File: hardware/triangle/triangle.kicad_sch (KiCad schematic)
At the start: 60 parts, among them J1 Conn_01x02_Socket, J2 Conn_01x02_Socket

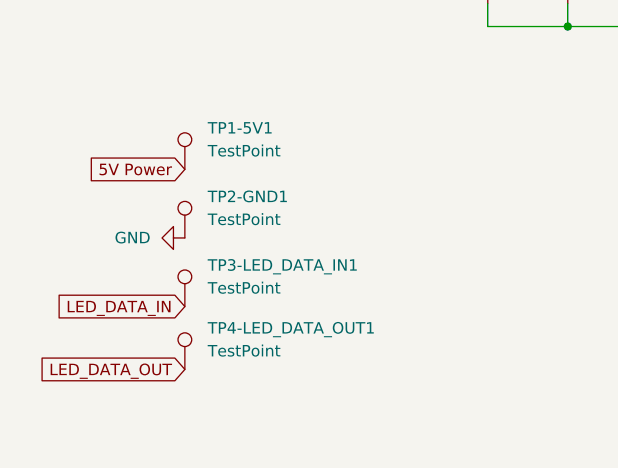
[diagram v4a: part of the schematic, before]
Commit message: remove unnecessary test pad and add silkscreen for sockets
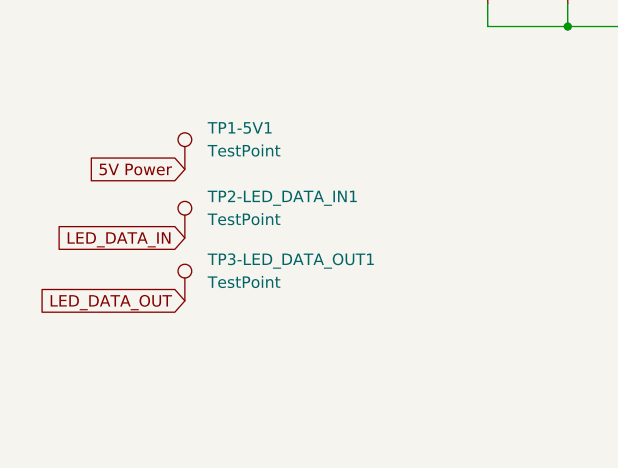
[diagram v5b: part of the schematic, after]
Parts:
- removed TP2-GND1: TestPoint, TestPoint:TestPoint_Pad_1.0x1.0mm, symbol Connector:TestPoint
- renumbered TP3-LED_DATA_IN1 to TP2-LED_DATA_IN1, TP4-LED_DATA_OUT1 to TP3-LED_DATA_OUT1
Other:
- moved on the sheet: TP2-LED_DATA_IN1, TP3-LED_DATA_OUT1
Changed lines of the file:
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@@
 	(global_label "LED_DATA_OUT"
 		(shape input)
-		(at 35.56 181.61 180)
+		(at 35.56 173.99 180)
 		(fields_autoplaced yes)
 		(effects
@@
 		)
 		(property "Intersheetrefs" "${INTERSHEET_REFS}"
-			(at 19.1491 181.61 0)
+			(at 19.1491 173.99 0)
 			(hide yes)
 			(show_name no)
@@
 	(global_label "LED_DATA_IN"
 		(shape input)
-		(at 35.56 174.625 180)
+		(at 35.56 167.005 180)
 		(fields_autoplaced yes)
 		(effects
@@
 		)
 		(property "Intersheetrefs" "${INTERSHEET_REFS}"
-			(at 20.8424 174.625 0)
+			(at 20.8424 167.005 0)
 			(hide yes)
 			(show_name no)
@@
 	)
 	(symbol
-		(lib_id "Connector:TestPoint")
-		(at 35.56 167.005 0)
-		(unit 1)
-		(body_style 1)
-		(exclude_from_sim no)
-		(in_bom yes)
-		(on_board yes)
-		(in_pos_files yes)
-		(dnp no)
-		(fields_autoplaced yes)
-		(property "Reference" "TP2-GND1"
-			(at 38.1 162.4329 0)
-			(show_name no)
-			(do_not_autoplace no)
-			(effects
-				(font
-					(size 1.27 1.27)
-				)
-				(justify left)
-			)
-		)
-		(property "Value" "TestPoint"
-			(at 38.1 164.9729 0)
-			(show_name no)
-			(do_not_autoplace no)
-			(effects
-				(font
-					(size 1.27 1.27)
-				)
-				(justify left)
-			)
-		)
-		(property "Footprint" "TestPoint:TestPoint_Pad_1.0x1.0mm"
-			(at 40.64 167.005 0)
-			(hide yes)
-			(show_name no)
-			(do_not_autoplace no)
-			(effects
-				(font
-					(size 1.27 1.27)
-				)
-			)
-		)
-		(property "Datasheet" ""
-			(at 40.64 167.005 0)
-			(hide yes)
-			(show_name no)
-			(do_not_autoplace no)
-			(effects
-				(font
-					(size 1.27 1.27)
-				)
-			)
-		)
-		(property "Description" "test point"
-			(at 35.56 167.005 0)
-			(hide yes)
-			(show_name no)
-			(do_not_autoplace no)
-			(effects
-				(font
-					(size 1.27 1.27)
-				)
-			)
-		)
-		(pin "1"
-		)
-		(instances
-			(project "triangle"
-				(path "/f9839f04-8b32-4f6f-9cb5-92c3ed04dc78"
-					(reference "TP2-GND1")
-					(unit 1)
-				)
-			)
-		)
-	)
-	(symbol
 		(lib_id "Mechanical:MountingHole")
 		(at 100.965 181.61 0)
@@
 	)
 	(symbol
-		(lib_id "power:GND")
-		(at 35.56 167.005 270)
-		(unit 1)
-		(body_style 1)
-		(exclude_from_sim no)
-		(in_bom yes)
-		(on_board yes)
-		(in_pos_files yes)
-		(dnp no)
-		(fields_autoplaced yes)
-		(property "Reference" "#PWR02"
-			(at 29.21 167.005 0)
-			(hide yes)
-			(show_name no)
-			(do_not_autoplace no)
-			(effects
-				(font
-					(size 1.27 1.27)
-				)
-			)
-		)
-		(property "Value" "GND"
-			(at 31.75 167.0049 90)
-			(show_name no)
-			(do_not_autoplace no)
-			(effects
-				(font
-					(size 1.27 1.27)
-				)
-				(justify right)
-			)
-		)
-		(property "Footprint" ""
-			(at 35.56 167.005 0)
-			(hide yes)
-			(show_name no)
-			(do_not_autoplace no)
-			(effects
-				(font
-					(size 1.27 1.27)
-				)
-			)
-		)
-		(property "Datasheet" ""
-			(at 35.56 167.005 0)
-			(hide yes)
-			(show_name no)
-			(do_not_autoplace no)
-			(effects
-				(font
-					(size 1.27 1.27)
-				)
-			)
-		)
-		(property "Description" "Power symbol creates a global label with name \"GND\" , ground"
-			(at 35.56 167.005 0)
-			(hide yes)
-			(show_name no)
-			(do_not_autoplace no)
-			(effects
-				(font
-					(size 1.27 1.27)
-				)
-			)
-		)
-		(pin "1"
-		)
-		(instances
-			(project "triangle"
-				(path "/f9839f04-8b32-4f6f-9cb5-92c3ed04dc78"
-					(reference "#PWR02")
-					(unit 1)
-				)
-			)
-		)
-	)
-	(symbol
 		(lib_id "Device:R")
 		(at 57.15 37.465 90)
@@
 	(symbol
 		(lib_id "Connector:TestPoint")
-		(at 35.56 181.61 0)
+		(at 35.56 173.99 0)
 		(unit 1)
 		(body_style 1)
@@
 		(dnp no)
 		(fields_autoplaced yes)
-		(property "Reference" "TP4-LED_DATA_OUT1"
-			(at 38.1 177.0379 0)
+		(property "Reference" "TP3-LED_DATA_OUT1"
+			(at 38.1 169.4179 0)
 			(show_name no)
 			(do_not_autoplace no)
@@
 		)
 		(property "Value" "TestPoint"
-			(at 38.1 179.5779 0)
+			(at 38.1 171.9579 0)
 			(show_name no)
 			(do_not_autoplace no)
@@
 		)
 		(property "Footprint" "TestPoint:TestPoint_Pad_1.0x1.0mm"
-			(at 40.64 181.61 0)
+			(at 40.64 173.99 0)
 			(hide yes)
 			(show_name no)
@@
 		)
 		(property "Datasheet" ""
-			(at 40.64 181.61 0)
+			(at 40.64 173.99 0)
 			(hide yes)
 			(show_name no)
@@
 		)
 		(property "Description" "test point"
-			(at 35.56 181.61 0)
+			(at 35.56 173.99 0)
 			(hide yes)
 			(show_name no)
@@
 			(project "triangle"
 				(path "/f9839f04-8b32-4f6f-9cb5-92c3ed04dc78"
-					(reference "TP4-LED_DATA_OUT1")
+					(reference "TP3-LED_DATA_OUT1")
 					(unit 1)
 				)
@@
 	(symbol
 		(lib_id "Connector:TestPoint")
-		(at 35.56 174.625 0)
+		(at 35.56 167.005 0)
 		(unit 1)
 		(body_style 1)
@@
 		(dnp no)
 		(fields_autoplaced yes)
-		(property "Reference" "TP3-LED_DATA_IN1"
-			(at 38.1 170.0529 0)
+		(property "Reference" "TP2-LED_DATA_IN1"
+			(at 38.1 162.4329 0)
 			(show_name no)
 			(do_not_autoplace no)
@@
 		)
 		(property "Value" "TestPoint"
-			(at 38.1 172.5929 0)
+			(at 38.1 164.9729 0)
 			(show_name no)
 			(do_not_autoplace no)
@@
 		)
 		(property "Footprint" "TestPoint:TestPoint_Pad_1.0x1.0mm"
-			(at 40.64 174.625 0)
+			(at 40.64 167.005 0)
 			(hide yes)
 			(show_name no)
@@
 		)
 		(property "Datasheet" ""
-			(at 40.64 174.625 0)
+			(at 40.64 167.005 0)
 			(hide yes)
 			(show_name no)
@@
 		)
 		(property "Description" "test point"
-			(at 35.56 174.625 0)
+			(at 35.56 167.005 0)
 			(hide yes)
 			(show_name no)
@@
 			(project "triangle"
 				(path "/f9839f04-8b32-4f6f-9cb5-92c3ed04dc78"
-					(reference "TP3-LED_DATA_IN1")
+					(reference "TP2-LED_DATA_IN1")
 					(unit 1)
 				)

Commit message: holes only.
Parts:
- H1, H2, H3: footprint footprints:SMD_BD5.6-L5.6-W5.6-D4.1 -> MountingHole:MountingHole_3.2mm_M3; JLCPCB Part # C5301783 -> (none)
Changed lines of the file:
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@@
 			)
 		)
-		(property "Footprint" "footprints:SMD_BD5.6-L5.6-W5.6-D4.1"
+		(property "Footprint" "MountingHole:MountingHole_3.2mm_M3"
 			(at 100.965 181.61 0)
 			(hide yes)
@@
 			)
 		)
-		(property "Datasheet" "https://www.lcsc.com/product-detail/C5301783.html"
+		(property "Datasheet" ""
 			(at 100.965 181.61 0)
 			(hide yes)
@@
 			)
 		)
-		(property "JLCPCB Part #" "C5301783"
+		(property "JLCPCB Part #" ""
 			(at 100.965 181.61 0)
 			(hide yes)
@@
 			)
 		)
-		(property "Footprint" "footprints:SMD_BD5.6-L5.6-W5.6-D4.1"
+		(property "Footprint" "MountingHole:MountingHole_3.2mm_M3"
 			(at 100.965 167.64 0)
 			(hide yes)
@@
 			)
 		)
-		(property "Datasheet" "https://www.lcsc.com/product-detail/C5301783.html"
+		(property "Datasheet" ""
 			(at 100.965 167.64 0)
 			(hide yes)
@@
 			)
 		)
-		(property "JLCPCB Part #" "C5301783"
+		(property "JLCPCB Part #" ""
 			(at 100.965 167.64 0)
 			(hide yes)
@@
 			)
 		)
-		(property "Footprint" "footprints:SMD_BD5.6-L5.6-W5.6-D4.1"
+		(property "Footprint" "MountingHole:MountingHole_3.2mm_M3"
 			(at 100.965 174.625 0)
 			(hide yes)
@@
 			)
 		)
-		(property "Datasheet" "https://www.lcsc.com/product-detail/C5301783.html"
+		(property "Datasheet" ""
 			(at 100.965 174.625 0)
 			(hide yes)
@@
 			)
 		)
-		(property "JLCPCB Part #" "C5301783"
+		(property "JLCPCB Part #" ""
 			(at 100.965 174.625 0)
 			(hide yes)

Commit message: updating components on triangle board - in progress
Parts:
- removed J1: Conn_01x02_Socket, footprints:CONN-SMD_B2B-PH-SM4-TBT-LF-SN, symbol Connector:Conn_01x02_Socket
- removed J2: Conn_01x02_Socket, footprints:CONN-SMD_ZX-XH2.54-2PLT, symbol Connector:Conn_01x02_Socket
- added J1, J2: USB_C_Receptacle_USB2.0_16P, footprints:TYPE-C-SMD_USB4120-03-C, symbol Connector:USB_C_Receptacle_USB2.0_16P
- added R5, R6, R7, R8: 5.1kΩ, Resistor_SMD:R_0603_1608Metric, symbol Device:R
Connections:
- net 5V Power: no longer C25.1
- net GND: now also C25.1, J1.A1 (GND), J1.A12 (GND), J1.B1 (GND), J1.B12 (GND), J1.SH (SHIELD), J2.A1 (GND), J2.A12 (GND), J2.B1 (GND), J2.B12 (GND), J2.SH (SHIELD), R5.1, R6.1, R7.1, R8.1
- net LED_DATA_IN: now also J1.A6 (D+), J1.A7 (D-), J1.B6 (D+), J1.B7 (D-)
- net LED_DATA_OUT: now also J2.A6 (D+), J2.A7 (D-), J2.B6 (D+), J2.B7 (D-)
- net 12V Power: now reaches C25.2
- net 12V Power: now also J1.A4 (VBUS), J1.A9 (VBUS), J1.B4 (VBUS), J1.B9 (VBUS), J2.A4 (VBUS), J2.A9 (VBUS), J2.B4 (VBUS), J2.B9 (VBUS)
- new net: J1.B5 (CC2), R6.2
- new net: J1.A5 (CC1), R5.2
- new net: J2.A5 (CC1), R7.2
- new net: J2.B5 (CC2), R8.2
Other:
- moved on the sheet: C1, C10, C11, C12, C13, C14, C15, C16, C17, C18, C19, C2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

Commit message: trying and failing to fix the usb-c
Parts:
- TP1-5V1, TP2-LED_DATA_IN1, TP3-LED_DATA_OUT1: footprint TestPoint:TestPoint_Pad_1.0x1.0mm -> TestPoint:TestPoint_Pad_D2.0mm
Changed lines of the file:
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@@
 			)
 		)
-		(property "Footprint" "TestPoint:TestPoint_Pad_1.0x1.0mm"
+		(property "Footprint" "TestPoint:TestPoint_Pad_D2.0mm"
 			(at 46.99 39.37 0)
 			(hide yes)
@@
 			)
 		)
-		(property "Footprint" "TestPoint:TestPoint_Pad_1.0x1.0mm"
+		(property "Footprint" "TestPoint:TestPoint_Pad_D2.0mm"
 			(at 46.99 53.975 0)
 			(hide yes)
@@
 			)
 		)
-		(property "Footprint" "TestPoint:TestPoint_Pad_1.0x1.0mm"
+		(property "Footprint" "TestPoint:TestPoint_Pad_D2.0mm"
 			(at 46.99 46.99 0)
 			(hide yes)
